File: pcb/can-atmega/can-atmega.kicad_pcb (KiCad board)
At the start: 2 copper layers, 36.6 x 46.5 mm, 31 parts, among them J1 Screw_Terminal_01x02, J2 Screw_Terminal_01x02, J3 Conn_01x04_Female, J4 Conn_01x02_Female, J5 Conn_01x08_Female, U1 LM1117-5.0, U2 TJA1051T, U3 MCP2515-xSO, U4 ATmega328P-A, X1 16MHz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

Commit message: motor module
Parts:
- removed J5: Conn_01x08_Female, Connector_PinSocket_2.54mm:PinSocket_1x08_P2.54mm_Vertical
- C1, C10, C11, C12, C3, C4, C5, C6, C7, C9: footprint Capacitor_SMD_Custom:C_KEM_0805_2.0x1.25mm -> Capacitor_SMD:C_1206_3216Metric
- C2, C8: footprint Capacitor_SMD_Custom:C_TAJ_3516_Bauform_A -> Capacitor_SMD:C_1206_3216Metric
- J4: value Conn_01x02_Female -> Connector_female; footprint Connector_PinSocket_2.54mm:PinSocket_1x02_P2.54mm_Vertical -> CAN_ATmega:Connector_female
- LED1: footprint LED_SMD_Custom:LED_EL_0603_GR1_1608 -> LED_SMD:LED_0805_2012Metric
- R1, R2, R3: footprint Resistors_SMD_Custom:R_SPR-0603_1.6x0.8mm -> Resistor_SMD:R_0805_2012Metric
- moved R1 40.2 mm to (168.7, 114.6), turned to 180 degrees
- moved LED1 34.4 mm to (163.6, 114.6), turned to 0 degrees
- moved J4 34.2 mm to (157.5, 99.1)
- moved C6 30.0 mm to (152.4, 84.8), turned to -90 degrees
- moved R3 26.5 mm to (163.8, 99.8)
- moved REF** 25.6 mm to (174.8, 71.6)
- moved REF** 25.4 mm to (142.8, 71.6)
- moved C4 25.4 mm to (165.9, 92.7)
- moved C3 25.1 mm to (162.6, 92.7)
- moved REF** 25.1 mm to (174.8, 113.6)
- moved J1 25.0 mm to (149.9, 73.7)
- moved J2 25.0 mm to (162.6, 73.7)
- moved J3 25.0 mm to (142.2, 78.7)
- moved U1 25.0 mm to (164.1, 86.6)
- moved U2 25.0 mm to (174.2, 84.4)
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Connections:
- J1 pad 1: /12V -> +12V
- J4 pad 1: +5V -> +12V
- J4 pad 2: GND -> +5V
- U1 pad 3: /12V -> +12V
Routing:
- net GND: track 24.4 -> 70.4 mm, vias 5 -> 12
- net +5V: track 124.3 -> 167.7 mm
- net +12V: track 0.00 -> 42.1 mm
- net /12V: track 20.7 -> 0.00 mm
- net U4_RXD: track 44.9 -> 51.4 mm
- net U4_RTS: track 35.6 -> 30.6 mm
- net /U4_RESET: track 4.64 -> 7.69 mm
- net /LED1: track 1.70 -> 3.23 mm
- net /U3_OSC_1: track 15.6 -> 16.5 mm
- net U4_TXD: track 36.6 -> 35.9 mm
- net /U4_OSC_1: track 13.2 -> 13.8 mm
- net /U4_OSC_2: track 11.3 -> 11.8 mm
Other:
- board size 36.6 x 46.5 mm -> 37 x 47 mm
- board text removed: "5V"
- board text removed: "A0"
- board text removed: "A1"
- board text removed: "A2"
- board text removed: "A3"
- board text removed: "D3"
- board text removed: "D4"
- board text removed: "D5"
- board text removed: "D6"

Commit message: update pcb
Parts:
- J1, J2: footprint TerminalBlock:TerminalBlock_bornier-2_P5.08mm -> TerminalBlock_Phoenix:TerminalBlock_Phoenix_MKDS-1,5-2-5.08_1x02_P5.08mm_Horizontal
- moved J1 5.10 mm to (154.9, 74.1), turned to 180 degrees
- moved J2 5.10 mm to (167.6, 74.1), turned to 180 degrees
- moved U2 0.54 mm to (173.7, 84.4)
- moved LED1 0.36 mm to (163.6, 114.2)
- moved R1 0.36 mm to (168.7, 114.2)
- renumbered J4 to J4-A
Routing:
- net U4_RXD: track 51.4 -> 34.8 mm, vias 0 -> 2
- net /CAN_H: track 21.3 -> 10.1 mm
- net GND: track 70.4 -> 80.9 mm
- net +12V: track 42.1 -> 39.6 mm
- net /CAN_L: track 16.9 -> 18.1 mm
- net /U2_U3_RXD: track 11.5 -> 10.9 mm
- net /U2_U3_TXD: track 3.43 -> 2.88 mm
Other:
- board text added: "12V Input"
- board text added: "CAN Input"
- board text added: "CAN_H"
- board text added: "CAN_L"
- board text added: "J4-B"
- board text added: "VIN"

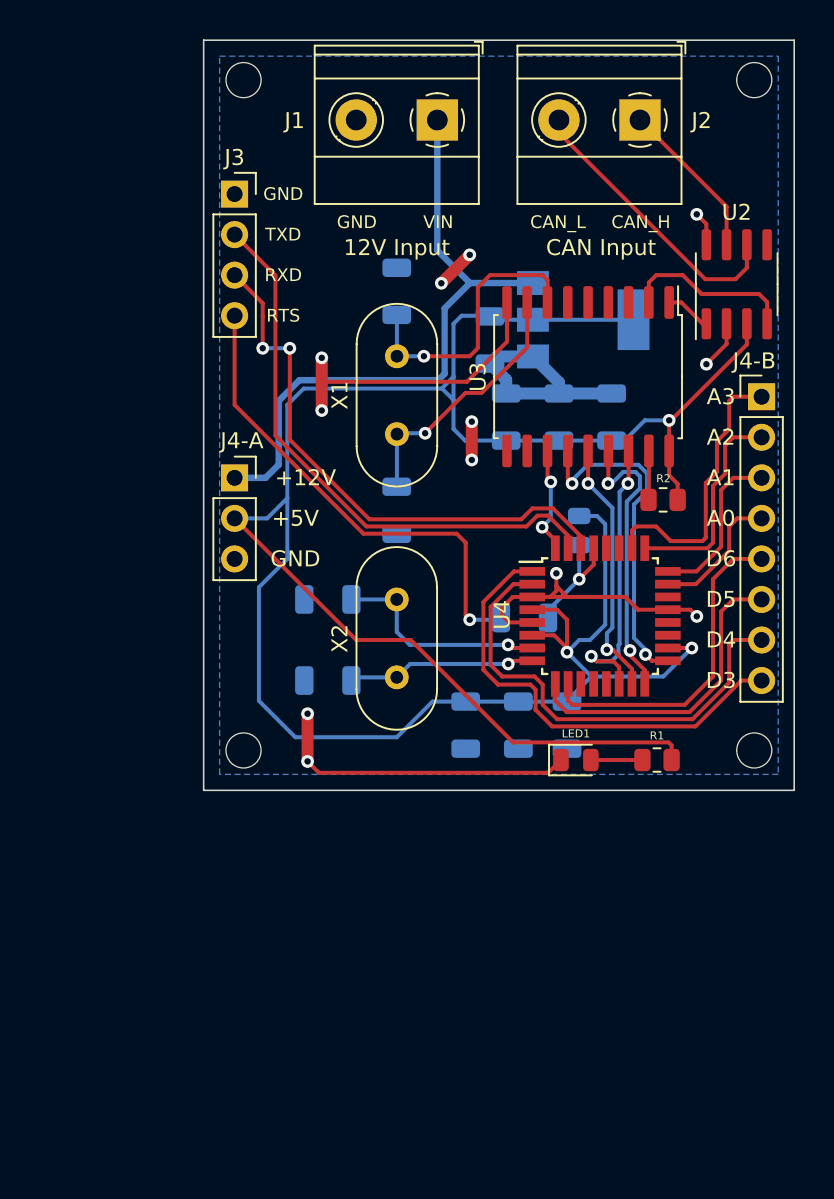
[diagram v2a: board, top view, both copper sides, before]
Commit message: added AVRISP adapter to pcb
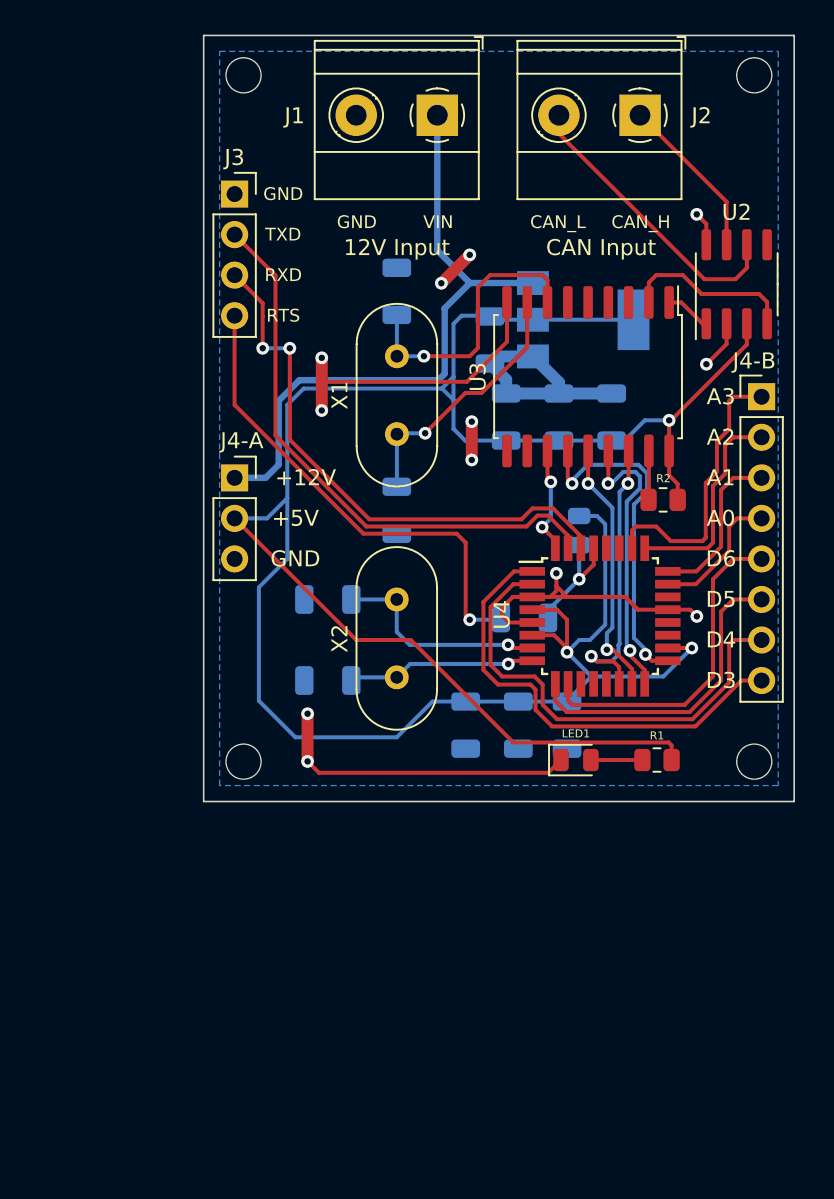
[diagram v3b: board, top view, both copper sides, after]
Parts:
- moved REF** 0.70 mm to (174.8, 114.3)
- moved REF** 0.70 mm to (142.8, 114.3)
- moved J1 0.30 mm to (154.9, 73.8)
- moved J2 0.30 mm to (167.6, 73.8)
- moved REF** 0.30 mm to (174.8, 71.3)
- moved REF** 0.30 mm to (142.8, 71.3)
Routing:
- net /CAN_L: track 18.1 -> 19.3 mm
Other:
- board size 37 x 47 mm -> 37 x 48 mm
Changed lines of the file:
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@@
   )
   (footprint "TerminalBlock_Phoenix:TerminalBlock_Phoenix_MKDS-1,5-2-5.08_1x02_P5.08mm_Horizontal" (layer "F.Cu")
-    (at 167.64 74.1 180)
+    (at 167.64 73.8 180)
     (descr "Terminal Block Phoenix MKDS-1,5-2-5.08, 2 pins, pitch 5.08mm, size 10.2x9.8mm^2, drill diamater 1.3mm, pad diameter 2.6mm, see http://www.farnell.com/datasheets/100425.pdf, script-generated using https://github.com/pointhi/kicad-footprint-generator/scripts/TerminalBlock_Phoenix")
     (tags "THT Terminal Block Phoenix MKDS-1,5-2-5.08 pitch 5.08mm size 10.2x9.8mm^2 drill 1.3mm pad 2.6mm")
@@
       (effects (font (size 1 1) (thickness 0.15)))
     )
-    (fp_text value "Screw_Terminal_01x02" (at 2.54 5.66 180) (layer "F.Fab")
+    (fp_text value "Screw_Terminal_01x02" (at 2.54 5.66 180) (layer "F.Fab") hide
       (effects (font (size 1 1) (thickness 0.15)))
     )
@@
   )
   (footprint "MountingHole:MountingHole_2.2mm_M2" (layer "F.Cu")
-    (at 174.8 113.6)
+    (at 174.8 114.3)
     (descr "Mounting Hole 2.2mm, no annular, M2")
     (tags "mounting hole 2.2mm no annular m2")
@@
   )
   (footprint "TerminalBlock_Phoenix:TerminalBlock_Phoenix_MKDS-1,5-2-5.08_1x02_P5.08mm_Horizontal" (layer "F.Cu")
-    (at 154.94 74.1 180)
+    (at 154.94 73.8 180)
     (descr "Terminal Block Phoenix MKDS-1,5-2-5.08, 2 pins, pitch 5.08mm, size 10.2x9.8mm^2, drill diamater 1.3mm, pad diameter 2.6mm, see http://www.farnell.com/datasheets/100425.pdf, script-generated using https://github.com/pointhi/kicad-footprint-generator/scripts/TerminalBlock_Phoenix")
     (tags "THT Terminal Block Phoenix MKDS-1,5-2-5.08 pitch 5.08mm size 10.2x9.8mm^2 drill 1.3mm pad 2.6mm")
@@
       (effects (font (size 1 1) (thickness 0.15)))
     )
-    (fp_text value "Screw_Terminal_01x02" (at 2.54 5.66 180) (layer "F.Fab")
+    (fp_text value "Screw_Terminal_01x02" (at 2.54 5.66 180) (layer "F.Fab") hide
       (effects (font (size 1 1) (thickness 0.15)))
     )
@@
   )
   (footprint "MountingHole:MountingHole_2.2mm_M2" (layer "F.Cu")
-    (at 174.8 71.6)
+    (at 174.8 71.3)
     (descr "Mounting Hole 2.2mm, no annular, M2")
     (tags "mounting hole 2.2mm no annular m2")
@@
   )
   (footprint "MountingHole:MountingHole_2.2mm_M2" (layer "F.Cu")
-    (at 142.8 71.6)
+    (at 142.8 71.3)
     (descr "Mounting Hole 2.2mm, no annular, M2")
     (tags "mounting hole 2.2mm no annular m2")
@@
   )
   (footprint "MountingHole:MountingHole_2.2mm_M2" (layer "F.Cu")
-    (at 142.8 113.6)
+    (at 142.8 114.3)
     (descr "Mounting Hole 2.2mm, no annular, M2")
     (tags "mounting hole 2.2mm no annular m2")
@@
     )
   )
-  (gr_line (start 140.3 69.1) (end 140.3 116.1) (layer "Edge.Cuts") (width 0.1))
-  (gr_line (start 177.3 116.1) (end 177.3 69.1) (layer "Edge.Cuts") (width 0.1))
-  (gr_line (start 177.3 116.1) (end 140.3 116.1) (layer "Edge.Cuts") (width 0.1))
-  (gr_line (start 177.3 69.1) (end 140.3 69.1) (layer "Edge.Cuts") (width 0.1))
+  (gr_line (start 140.3 68.8) (end 140.3 116.8) (layer "Edge.Cuts") (width 0.1))
+  (gr_line (start 177.3 116.8) (end 177.3 68.8) (layer "Edge.Cuts") (width 0.1))
+  (gr_line (start 177.3 116.8) (end 140.3 116.8) (layer "Edge.Cuts") (width 0.1))
+  (gr_line (start 177.3 68.8) (end 140.3 68.8) (layer "Edge.Cuts") (width 0.1))
   (gr_text "CAN_H" (at 167.7 80.5) (layer "F.SilkS")
     (effects (font (size 0.8 0.8) (thickness 0.1)))
@@
   (segment (start 171.795 86.865) (end 171.565 86.865) (width 0.25) (layer "F.Cu") (net 31))
   (segment (start 171.565 86.865) (end 170.232 85.532) (width 0.25) (layer "F.Cu") (net 31))
-  (segment (start 154.94 82.268) (end 154.94 74.1) (width 0.4) (layer "B.Cu") (net 32))
   (segment (start 155 90.4) (end 155.4 90) (width 0.4) (layer "B.Cu") (net 32))
   (segment (start 145 91.7) (end 146.3 90.4) (width 0.4) (layer "B.Cu") (net 32))
@@
   (segment (start 142.24 96.52) (end 144.18 96.52) (width 0.4) (layer "B.Cu") (net 32))
   (segment (start 144.18 96.52) (end 145 95.7) (width 0.4) (layer "B.Cu") (net 32))
+  (segment (start 154.94 82.268) (end 154.94 73.8) (width 0.4) (layer "B.Cu") (net 32))
   (segment (start 155.4 90) (end 155.4 85.9) (width 0.4) (layer "B.Cu") (net 32))
   (segment (start 155.4 85.9) (end 156.986 84.314) (width 0.4) (layer "B.Cu") (net 32))
@@
   (segment (start 146.3 90.4) (end 155 90.4) (width 0.4) (layer "B.Cu") (net 32))
   (segment (start 154.94 82.268) (end 156.986 84.314) (width 0.4) (layer "B.Cu") (net 32))
-  (segment (start 173.065 81.915) (end 173.065 79.525) (width 0.25) (layer "F.Cu") (net 33))
-  (segment (start 173.065 79.525) (end 167.64 74.1) (width 0.25) (layer "F.Cu") (net 33))
+  (segment (start 173.065 81.915) (end 173.065 79.225) (width 0.25) (layer "F.Cu") (net 33))
+  (segment (start 173.065 79.225) (end 167.64 73.8) (width 0.25) (layer "F.Cu") (net 33))
+  (segment (start 162.56 74.96) (end 162.56 73.8) (width 0.25) (layer "F.Cu") (net 34))
+  (segment (start 173.626 84.074) (end 171.674 84.074) (width 0.25) (layer "F.Cu") (net 34))
+  (segment (start 162.56 74.9046) (end 162.56 74.1) (width 0.25) (layer "F.Cu") (net 34))
+  (segment (start 171.674 84.074) (end 162.56 74.96) (width 0.25) (layer "F.Cu") (net 34))
+  (segment (start 174.335 81.915) (end 174.335 83.365) (width 0.25) (layer "F.Cu") (net 34))
   (segment (start 174.335 83.365) (end 173.626 84.074) (width 0.25) (layer "F.Cu") (net 34))
-  (segment (start 162.56 74.9046) (end 162.56 74.1) (width 0.25) (layer "F.Cu") (net 34))
-  (segment (start 173.626 84.074) (end 171.7294 84.074) (width 0.25) (layer "F.Cu") (net 34))
-  (segment (start 174.335 81.915) (end 174.335 83.365) (width 0.25) (layer "F.Cu") (net 34))
-  (segment (start 171.7294 84.074) (end 162.56 74.9046) (width 0.25) (layer "F.Cu") (net 34))
   (segment (start 168.196 84.28) (end 168.656 83.82) (width 0.25) (layer "F.Cu") (net 35))
   (segment (start 175.605 85.505) (end 175.605 86.865) (width 0.25) (layer "F.Cu") (net 35))
@@
     (polygon
       (pts
-        (xy 176.3 115.1)
-        (xy 141.3 115.1)
-        (xy 141.3 70.1)
-        (xy 176.3 70.1)
+        (xy 176.3 115.8)
+        (xy 141.3 115.8)
+        (xy 141.3 69.8)
+        (xy 176.3 69.8)
       )
     )

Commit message: m12 plug; j1939 transition
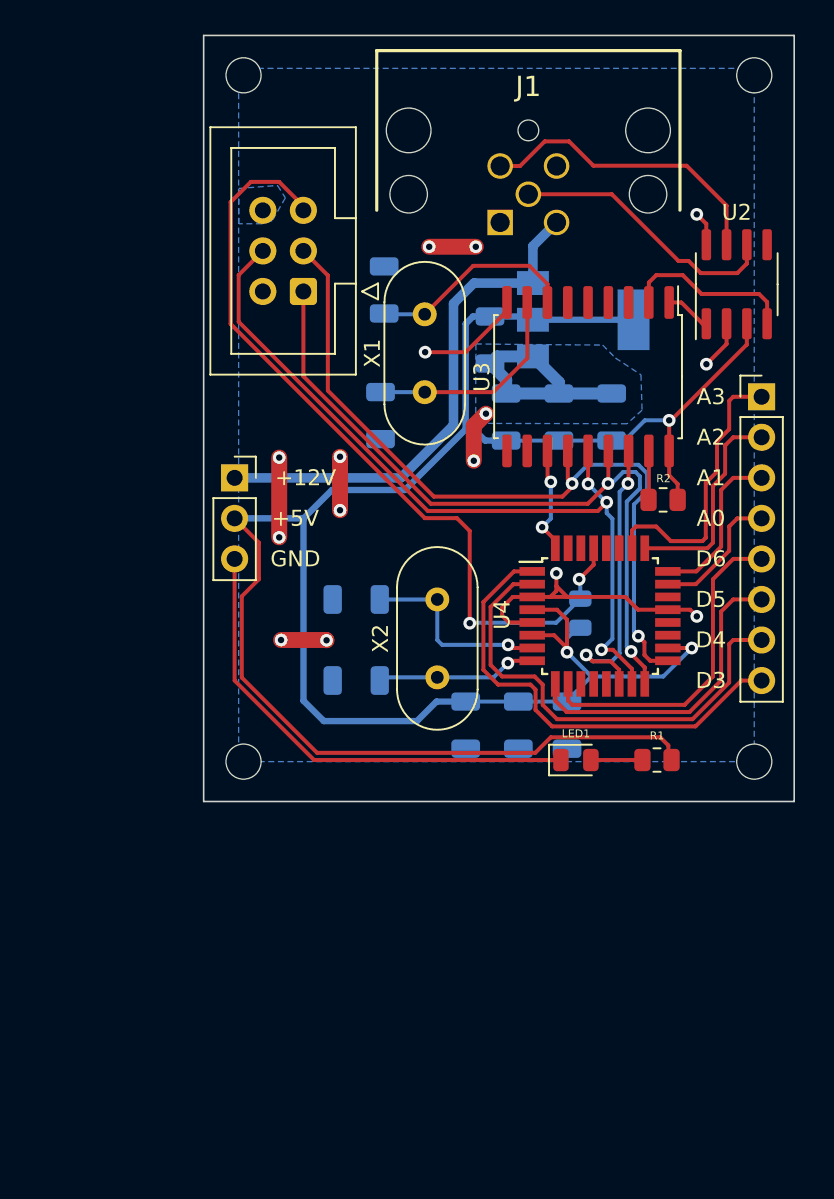
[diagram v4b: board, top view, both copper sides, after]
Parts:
- removed C12: 1uF, Capacitor_SMD:C_1206_3216Metric
- removed J2: Screw_Terminal_01x02, TerminalBlock_Phoenix:TerminalBlock_Phoenix_MKDS-1,5-2-5.08_1x02_P5.08mm_Horizontal
- removed J4-A: Connector_female, CAN_ATmega:Connector_female
- added J4: Connector_female, CAN_ATmega:Connector_female, F.Cu at (157.5, 99.1)
- J1: value Screw_Terminal_01x02 -> Screw_Terminal_01x05; footprint TerminalBlock_Phoenix:TerminalBlock_Phoenix_MKDS-1,5-2-5.08_1x02_P5.08mm_Horizontal -> mouser:4301207
- J3: value Conn_01x04_Female -> Conn_02x03_Odd_Even; footprint Connector_PinSocket_2.54mm:PinSocket_1x04_P2.54mm_Vertical -> Connector_IDC:IDC-Header_2x03_P2.54mm_Vertical
- moved J1 7.79 mm to (158.9, 80.5), turned to 0 degrees
- moved J3 7.47 mm to (146.5, 84.8), turned to 180 degrees
- moved C5 6.02 mm to (151.4, 92.6)
- moved R3 5.18 mm to (163.9, 105.0), turned to 90 degrees
- moved X1 3.15 mm to (154.2, 86.3)
- moved X2 2.54 mm to (154.9, 104.1)
- moved C10 1.78 mm to (149.9, 104.1)
- moved C11 1.78 mm to (149.9, 109.2)
- moved C6 0.79 mm to (151.6, 84.7)
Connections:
- net CS renamed D10_CS
- net INT renamed D2_INT
- J1 pad 1: +12V -> unconnected-(J1-Pad1)
- J1 pad 2: GND -> +12V
- J3 pad 1: GND -> U4_D12_MISO
- J3 pad 2: U4_TXD -> unconnected-(J3-Pad2)
- J3 pad 3: U4_RXD -> U4_D13_SCK
- J3 pad 4: U4_RTS -> U4_D11_MOSI
- R3 pad 2: /U4_RESET -> U4_RST
- U2 pad 6: /CAN_L -> CAN_L
- U2 pad 7: /CAN_H -> CAN_H
- U3 pad 13: SCK -> U4_D13_SCK
- U3 pad 14: SI -> U4_D11_MOSI
- U3 pad 15: SO -> U4_D12_MISO
- U4 pad 15: SI -> U4_D11_MOSI
- U4 pad 16: SO -> U4_D12_MISO
- U4 pad 17: SCK -> U4_D13_SCK
- U4 pad 29: /U4_RESET -> U4_RST
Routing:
- net U4_RST: track 0.00 -> 50.9 mm, vias 0 -> 2
- net U4_D11_MOSI: track 0.00 -> 50.0 mm, vias 0 -> 3
- net U4_D13_SCK: track 0.00 -> 49.2 mm, vias 0 -> 2
- net U4_D12_MISO: track 0.00 -> 46.5 mm, vias 0 -> 2
- net U4_TXD: track 35.9 -> 0.00 mm
- net U4_RXD: track 34.8 -> 0.00 mm, vias 2 -> 0
- net U4_RTS: track 30.6 -> 0.00 mm, vias 1 -> 0
- net SCK: track 21.2 -> 0.00 mm, vias 2 -> 0
- net /CAN_L: track 19.3 -> 0.00 mm
- net CAN_H: track 0.00 -> 18.9 mm
- net SO: track 18.3 -> 0.00 mm, vias 2 -> 0
- net CAN_L: track 0.00 -> 17.2 mm
- net SI: track 16.2 -> 0.00 mm, vias 2 -> 0
- net +5V: track 167.9 -> 153.7 mm
- net GND: track 80.9 -> 92.4 mm, vias 12 -> 15
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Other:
- board text removed: "12V Input"
- board text removed: "CAN Input"
- board text removed: "CAN_H"
- board text removed: "CAN_L"
- board text removed: "GND"
- board text removed: "J4-B"
- board text removed: "RTS"
- board text removed: "RXD"
- board text removed: "TXD"
- board text removed: "VIN"
